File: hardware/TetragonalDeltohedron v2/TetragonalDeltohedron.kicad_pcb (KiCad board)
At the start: 2 copper layers, 56.3 x 80 mm, 72 parts, among them U1 XL-0807RGBC-WS2812B, U10 XL-0807RGBC-WS2812B, U2 XL-0807RGBC-WS2812B, U3 XL-0807RGBC-WS2812B, U4 XL-0807RGBC-WS2812B, U5 XL-0807RGBC-WS2812B, U6 XL-0807RGBC-WS2812B, U7 XL-0807RGBC-WS2812B, U8 XL-0807RGBC-WS2812B, U9 XL-0807RGBC-WS2812B

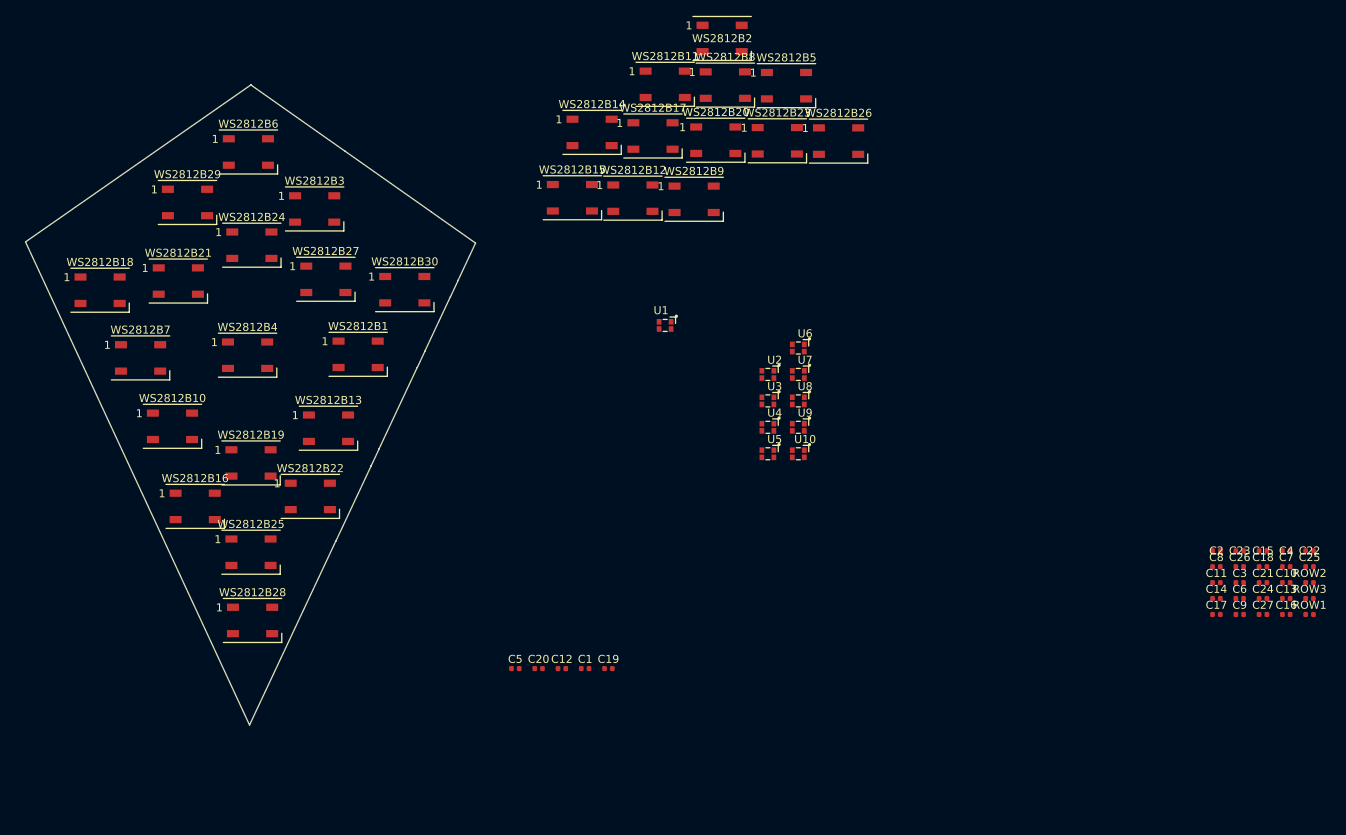
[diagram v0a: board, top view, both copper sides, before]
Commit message: Adding all the components to the PCB
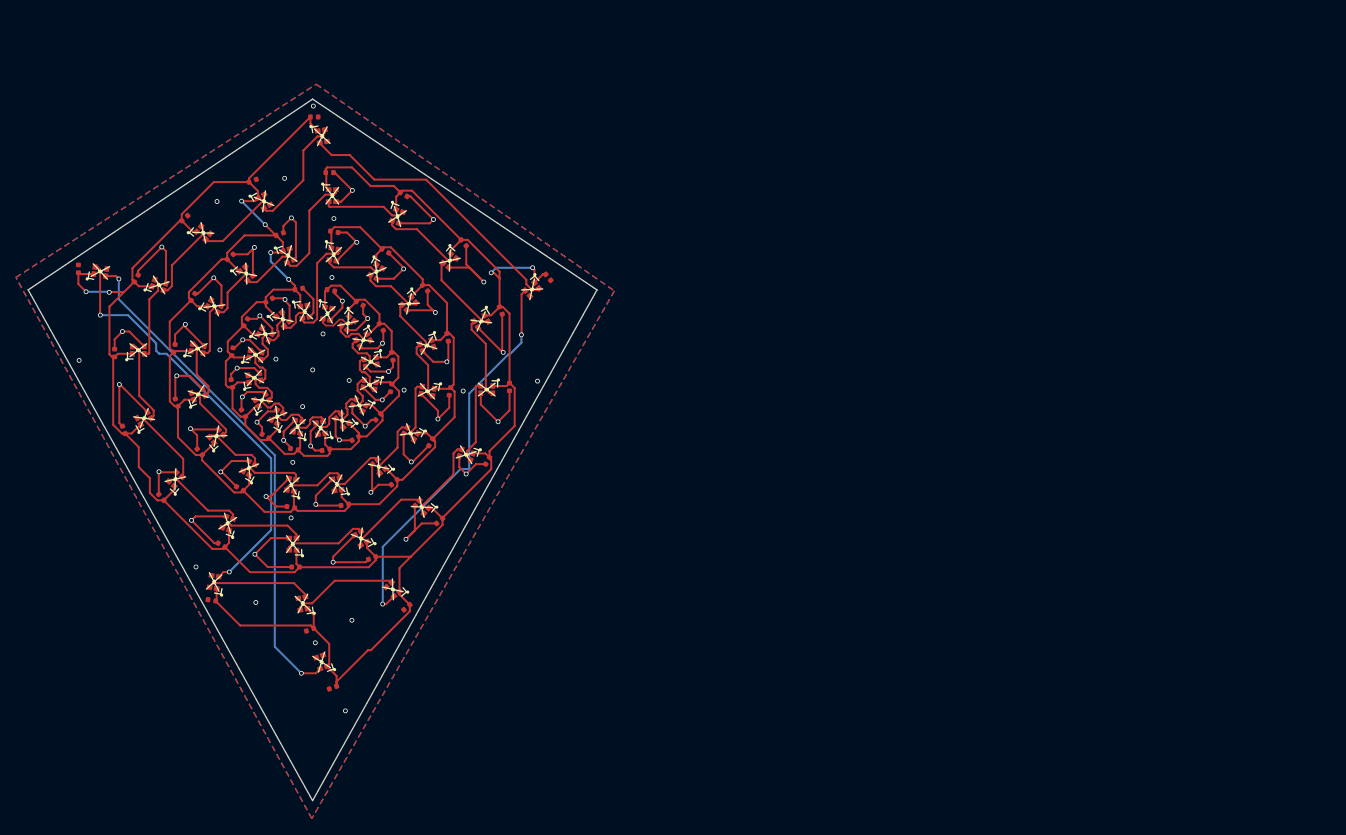
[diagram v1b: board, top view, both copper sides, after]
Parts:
- removed the G*** at (37.0, 59.9) (x2)
- removed ROW1, ROW2, ROW3: 10uF,10V,X5R, SWS-Library:C_0402_1005Metric
- removed WS2812B1, WS2812B10, WS2812B11, WS2812B12, WS2812B13, WS2812B14, WS2812B15, WS2812B16, WS2812B17, WS2812B18, WS2812B19, WS2812B2, WS2812B20, WS2812B21, WS2812B22, WS2812B23, WS2812B24, WS2812B25, WS2812B26, WS2812B27, WS2812B28, WS2812B29, WS2812B3, WS2812B30, WS2812B4, WS2812B5, WS2812B6, WS2812B7, WS2812B8, WS2812B9: XL-5050RGBC-WS2812B, LED_SMD:LED_WS2812B_PLCC4_5.0x5.0mm_P3.2mm
- added C28: 1uF,25V,X5R, SWS-Library:C_0402_1005Metric, F.Cu at (32.9, 55.2)
- added C29: 1uF,25V,X5R, SWS-Library:C_0402_1005Metric, F.Cu at (32.6, 48.4)
- added C30: 1uF,25V,X5R, SWS-Library:C_0402_1005Metric, F.Cu at (35.0, 42.0)
- added C31: 1uF,25V,X5R, SWS-Library:C_0402_1005Metric, F.Cu at (39.6, 37.0)
- added C32: 1uF,25V,X5R, SWS-Library:C_0402_1005Metric, F.Cu at (45.8, 34.1)
- added C33: 1uF,25V,X5R, SWS-Library:C_0402_1005Metric, F.Cu at (52.0, 26.4)
- added C34: 1uF,25V,X5R, SWS-Library:C_0402_1005Metric, F.Cu at (61.3, 29.2)
- added C35: 1uF,25V,X5R, SWS-Library:C_0402_1005Metric, F.Cu at (68.8, 35.2)
- added C36: 1uF,25V,X5R, SWS-Library:C_0402_1005Metric, F.Cu at (73.5, 43.7)
- added C37: 1uF,25V,X5R, SWS-Library:C_0402_1005Metric, F.Cu at (74.5, 53.2)
- added C38: 1uF,25V,X5R, SWS-Library:C_0402_1005Metric, F.Cu at (71.8, 62.5)
- added C39: 1uF,25V,X5R, SWS-Library:C_0402_1005Metric, F.Cu at (65.8, 70.0)
- added C40: 1uF,25V,X5R, SWS-Library:C_0402_1005Metric, F.Cu at (57.4, 74.6)
- added C41: 1uF,25V,X5R, SWS-Library:C_0402_1005Metric, F.Cu at (47.8, 75.8)
- added C42: 1uF,25V,X5R, SWS-Library:C_0402_1005Metric, F.Cu at (38.5, 73.0)
- added C43: 1uF,25V,X5R, SWS-Library:C_0402_1005Metric, F.Cu at (31.0, 67.0)
- added C44: 1uF,25V,X5R, SWS-Library:C_0402_1005Metric, F.Cu at (26.3, 58.6)
- added C45: 1uF,25V,X5R, SWS-Library:C_0402_1005Metric, F.Cu at (25.2, 49.0)
- added C46: 1uF,25V,X5R, SWS-Library:C_0402_1005Metric, F.Cu at (27.9, 39.7)
- added C47: 1uF,25V,X5R, SWS-Library:C_0402_1005Metric, F.Cu at (33.9, 32.1)
- added C48: 1uF,25V,X5R, SWS-Library:C_0402_1005Metric, F.Cu at (42.4, 27.5)
- added C49: 1uF,25V,X5R, SWS-Library:C_0402_1005Metric, F.Cu at (50.1, 19.5)
- added C50: 1uF,25V,X5R, SWS-Library:C_0402_1005Metric, F.Cu at (79.4, 39.5)
- added C51: 1uF,25V,X5R, SWS-Library:C_0402_1005Metric, F.Cu at (61.7, 80.8)
- added C52: 1uF,25V,X5R, SWS-Library:C_0402_1005Metric, F.Cu at (49.6, 83.6)
- added C53: 1uF,25V,X5R, SWS-Library:C_0402_1005Metric, F.Cu at (37.3, 79.9)
- added C54: 1uF,25V,X5R, SWS-Library:C_0402_1005Metric, F.Cu at (20.6, 38.5)
- added C55: 1uF,25V,X5R, SWS-Library:C_0402_1005Metric, F.Cu at (52.5, 90.8)
- added G***: LOGO, LOGO, F.Cu at (48.6, 57.5)
- added U11: XL-0807RGBC-WS2812B, SWS-Library:XL-0807RGBC-WS2812B, F.Cu at (43.6, 54.9)
- added U12: XL-0807RGBC-WS2812B, SWS-Library:XL-0807RGBC-WS2812B, F.Cu at (42.6, 52.1)
- added U13: XL-0807RGBC-WS2812B, SWS-Library:XL-0807RGBC-WS2812B, F.Cu at (42.8, 49.2)
- added U14: XL-0807RGBC-WS2812B, SWS-Library:XL-0807RGBC-WS2812B, F.Cu at (44.0, 46.6)
- added U15: XL-0807RGBC-WS2812B, SWS-Library:XL-0807RGBC-WS2812B, F.Cu at (46.2, 44.8)
- added U16: XL-0807RGBC-WS2812B, SWS-Library:XL-0807RGBC-WS2812B, F.Cu at (49.0, 43.8)
- added U17: XL-0807RGBC-WS2812B, SWS-Library:XL-0807RGBC-WS2812B, F.Cu at (52.6, 36.7)
- added U18: XL-0807RGBC-WS2812B, SWS-Library:XL-0807RGBC-WS2812B, F.Cu at (57.9, 38.9)
- added U19: XL-0807RGBC-WS2812B, SWS-Library:XL-0807RGBC-WS2812B, F.Cu at (62.0, 42.8)
- added U20: XL-0807RGBC-WS2812B, SWS-Library:XL-0807RGBC-WS2812B, F.Cu at (64.2, 48.1)
- added U21: XL-0807RGBC-WS2812B, SWS-Library:XL-0807RGBC-WS2812B, F.Cu at (64.3, 53.8)
- added U22: XL-0807RGBC-WS2812B, SWS-Library:XL-0807RGBC-WS2812B, F.Cu at (62.2, 59.1)
- added U23: XL-0807RGBC-WS2812B, SWS-Library:XL-0807RGBC-WS2812B, F.Cu at (58.2, 63.2)
- added U24: XL-0807RGBC-WS2812B, SWS-Library:XL-0807RGBC-WS2812B, F.Cu at (53.0, 65.4)
- added U25: XL-0807RGBC-WS2812B, SWS-Library:XL-0807RGBC-WS2812B, F.Cu at (47.3, 65.5)
- added U26: XL-0807RGBC-WS2812B, SWS-Library:XL-0807RGBC-WS2812B, F.Cu at (42.0, 63.4)
- added U27: XL-0807RGBC-WS2812B, SWS-Library:XL-0807RGBC-WS2812B, F.Cu at (37.9, 59.4)
- added U28: XL-0807RGBC-WS2812B, SWS-Library:XL-0807RGBC-WS2812B, F.Cu at (35.6, 54.2)
- added U29: XL-0807RGBC-WS2812B, SWS-Library:XL-0807RGBC-WS2812B, F.Cu at (35.6, 48.5)
- added U30: XL-0807RGBC-WS2812B, SWS-Library:XL-0807RGBC-WS2812B, F.Cu at (37.7, 43.1)
- added U31: XL-0807RGBC-WS2812B, SWS-Library:XL-0807RGBC-WS2812B, F.Cu at (41.6, 39.1)
- added U32: XL-0807RGBC-WS2812B, SWS-Library:XL-0807RGBC-WS2812B, F.Cu at (46.9, 36.8)
- added U33: XL-0807RGBC-WS2812B, SWS-Library:XL-0807RGBC-WS2812B, F.Cu at (52.4, 29.3)
- added U34: XL-0807RGBC-WS2812B, SWS-Library:XL-0807RGBC-WS2812B, F.Cu at (60.5, 31.9)
- added U35: XL-0807RGBC-WS2812B, SWS-Library:XL-0807RGBC-WS2812B, F.Cu at (67.1, 37.5)
- added U36: XL-0807RGBC-WS2812B, SWS-Library:XL-0807RGBC-WS2812B, F.Cu at (71.0, 45.1)
- added U37: XL-0807RGBC-WS2812B, SWS-Library:XL-0807RGBC-WS2812B, F.Cu at (71.7, 53.6)
- added U38: XL-0807RGBC-WS2812B, SWS-Library:XL-0807RGBC-WS2812B, F.Cu at (69.1, 61.7)
- added U39: XL-0807RGBC-WS2812B, SWS-Library:XL-0807RGBC-WS2812B, F.Cu at (63.6, 68.3)
- added U40: XL-0807RGBC-WS2812B, SWS-Library:XL-0807RGBC-WS2812B, F.Cu at (56.0, 72.2)
- added U41: XL-0807RGBC-WS2812B, SWS-Library:XL-0807RGBC-WS2812B, F.Cu at (47.5, 72.9)
- added U42: XL-0807RGBC-WS2812B, SWS-Library:XL-0807RGBC-WS2812B, F.Cu at (39.3, 70.3)
- added U43: XL-0807RGBC-WS2812B, SWS-Library:XL-0807RGBC-WS2812B, F.Cu at (32.8, 64.8)
- added U44: XL-0807RGBC-WS2812B, SWS-Library:XL-0807RGBC-WS2812B, F.Cu at (28.9, 57.2)
- added U45: XL-0807RGBC-WS2812B, SWS-Library:XL-0807RGBC-WS2812B, F.Cu at (28.1, 48.6)
- added U46: XL-0807RGBC-WS2812B, SWS-Library:XL-0807RGBC-WS2812B, F.Cu at (30.7, 40.5)
- added U47: XL-0807RGBC-WS2812B, SWS-Library:XL-0807RGBC-WS2812B, F.Cu at (36.3, 34.0)
- added U48: XL-0807RGBC-WS2812B, SWS-Library:XL-0807RGBC-WS2812B, F.Cu at (43.9, 30.1)
- added U49: XL-0807RGBC-WS2812B, SWS-Library:XL-0807RGBC-WS2812B, F.Cu at (51.1, 21.9)
- added U50: XL-0807RGBC-WS2812B, SWS-Library:XL-0807RGBC-WS2812B, F.Cu at (77.4, 41.1)
- added U51: XL-0807RGBC-WS2812B, SWS-Library:XL-0807RGBC-WS2812B, F.Cu at (60.0, 78.5)
- added U52: XL-0807RGBC-WS2812B, SWS-Library:XL-0807RGBC-WS2812B, F.Cu at (48.7, 80.3)
- added U53: XL-0807RGBC-WS2812B, SWS-Library:XL-0807RGBC-WS2812B, F.Cu at (37.6, 77.6)
- added U54: XL-0807RGBC-WS2812B, SWS-Library:XL-0807RGBC-WS2812B, F.Cu at (23.4, 38.8)
- added U55: XL-0807RGBC-WS2812B, SWS-Library:XL-0807RGBC-WS2812B, F.Cu at (51.0, 87.6)
- moved C13 135.3 mm to (39.9, 48.8), turned to 80 degrees
- moved C27 134.5 mm to (35.8, 61.4), turned to 130 degrees
- moved C16 130.0 mm to (48.2, 41.0), turned to 10 degrees
- moved C10 128.9 mm to (44.0, 59.4), turned to 150 degrees
- moved C15 128.1 mm to (44.5, 42.4), turned to 30 degrees
- moved C25 127.6 mm to (47.2, 68.3), turned to 170 degrees
- moved C14 126.2 mm to (41.6, 45.2), turned to 60 degrees
- moved C26 125.4 mm to (40.8, 66.0), turned to 150 degrees
- moved C11 123.5 mm to (41.3, 56.5), turned to 120 degrees
- moved C17 120.2 mm to (52.6, 33.9), turned to -10 degrees
- moved C9 120.0 mm to (47.6, 61.0), turned to 170 degrees
- moved C7 117.5 mm to (55.3, 59.7), turned to -150 degrees
- moved C18 116.6 mm to (59.0, 36.2), turned to -30 degrees
- moved C24 115.4 mm to (54.0, 68.0), turned to -170 degrees
- moved C4 114.4 mm to (59.9, 49.4), turned to -80 degrees
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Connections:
- U1 pad 4: Data-in -> DATA_IN
- U10 pad 2: ROW_02 -> Net-(U10-DOUT)
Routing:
- net +5V: track 0.00 -> 550.4 mm, vias 0 -> 8
- net GND: track 0.00 -> 303.3 mm, vias 0 -> 67
- net Net-(U54-DOUT): track 0.00 -> 63.1 mm, vias 0 -> 2
- net Net-(U53-DOUT): track 0.00 -> 53.7 mm, vias 0 -> 2
- net Net-(U50-DOUT): track 0.00 -> 49.3 mm, vias 0 -> 2
- net Net-(U49-DOUT): track 0.00 -> 35.4 mm
- net ROW_04: track 0.00 -> 14.3 mm
- net ROW_03: track 0.00 -> 13.6 mm
- net Net-(U51-DOUT): track 0.00 -> 13.2 mm
- net ROW_02: track 0.00 -> 13.1 mm
- net Net-(U52-DOUT): track 0.00 -> 13.1 mm
- net Net-(U33-DOUT): track 0.00 -> 10.5 mm
- net Net-(U45-DOUT): track 0.00 -> 10.5 mm
- net Net-(U34-DOUT): track 0.00 -> 10.5 mm
- net Net-(U42-DOUT): track 0.00 -> 10.5 mm
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- added copper zone on B.Cu, net GND
- added copper zone on F.Cu, net GND
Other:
- board size 56.3 x 80 mm -> 71.1 x 87.7 mm
